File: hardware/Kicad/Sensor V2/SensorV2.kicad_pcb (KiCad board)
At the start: 2 copper layers, 82.4 x 64 mm, 20 parts, among them J1 Controller Connector, J2 Conn_01x08, J3 Conn_01x08, J4 Conn_01x06, J5 Conn_01x06, J6 Conn_01x04, U1 2821, U4 MicroSD_Breakout

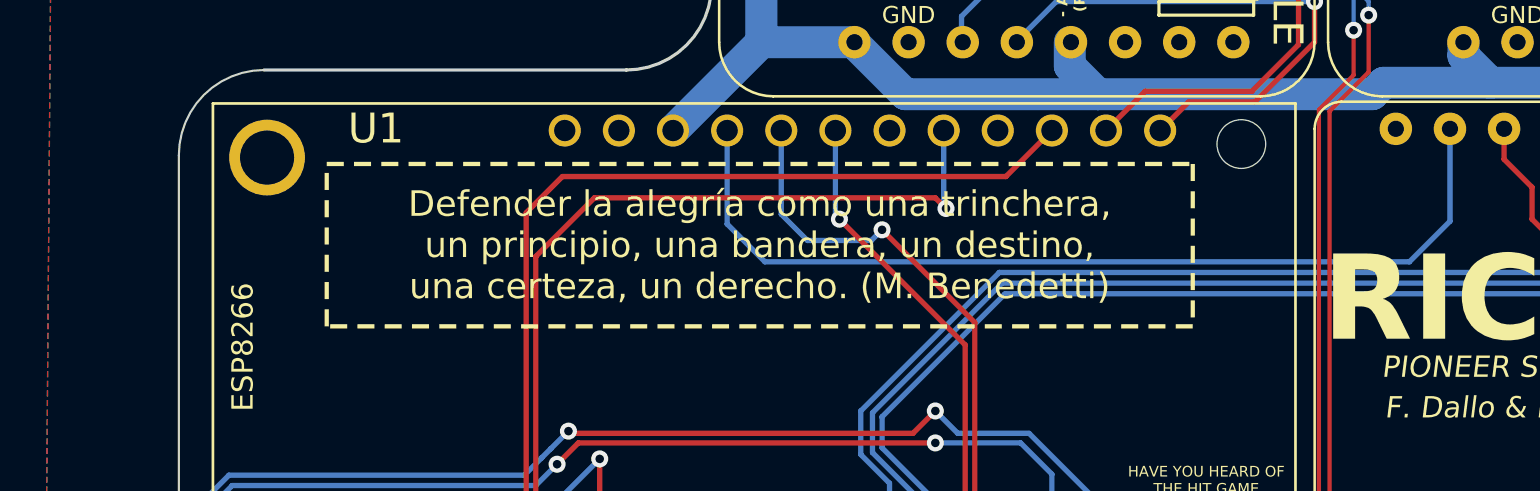
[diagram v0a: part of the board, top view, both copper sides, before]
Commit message: fixed CS to gpio16
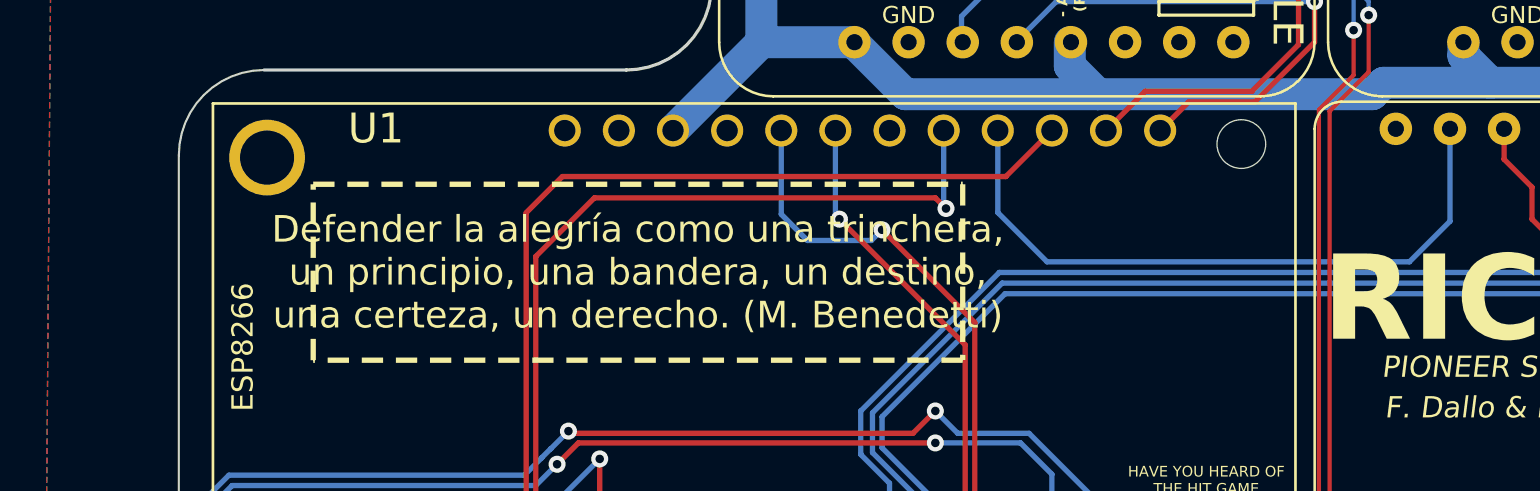
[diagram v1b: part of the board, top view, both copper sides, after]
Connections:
- U1 pad 20: /CS1 -> unconnected-(U1-GPIO14-Pad20)
- U1 pad 25: unconnected-(U1-GPIO16-Pad25) -> /CS1
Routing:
- net /CS1: track 44.2 -> 31.2 mm

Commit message: added some changes
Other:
- board text added: "ADC Addr: 0x49"
- board text removed: "ADC Addr: 0x40"
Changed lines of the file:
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@@
     (effects (font (size 0.8 0.8) (thickness 0.15)))
+  )
+  (gr_text "RX(Board)" (at 28.575 130.81) (layer "F.SilkS")
+    (effects (font (size 0.8 0.8) (thickness 0.15)))
+  )
+  (gr_text "F. Dallo & N. Zhao" (at 83.82 116.84) (layer "F.SilkS")
+    (effects (font (size 1 1) (thickness 0.15) italic))
+  )
+  (gr_text "RTC Only" (at 97.79 97.155) (layer "F.SilkS")
+    (effects (font (size 0.8 0.8) (thickness 0.15)))
+  )
+  (gr_text "- ADDR \n     (RTC NC)" (at 62.865 97.155 90) (layer "F.SilkS")
+    (effects (font (size 0.5 0.5) (thickness 0.1) bold))
+  )
+  (gr_text "ADC Addr: 0x48" (at 88.265 89.535) (layer "F.SilkS")
+    (effects (font (size 1.5 1.5) (thickness 0.25) bold))
+  )
+  (gr_text "TO MAIN" (at 21.59 131.445 270) (layer "F.SilkS")
+    (effects (font (size 1 1) (thickness 0.15)))
+  )
+  (gr_text "GND" (at 40.005 132.715) (layer "F.SilkS")
+    (effects (font (size 0.8 0.8) (thickness 0.15)))
+  )
+  (gr_text "GND" (at 83.82 98.425) (layer "F.SilkS")
+    (effects (font (size 0.8 0.8) (thickness 0.15)))
+  )
+  (gr_text "ADC MODULE" (at 73.025 93.345 270) (layer "F.SilkS")
+    (effects (font (size 1.4 1.4) (thickness 0.2)))
   )
   (gr_text "- ADDR \n     (RTC NC)" (at 91.44 97.155 90) (layer "F.SilkS")
     (effects (font (size 0.5 0.5) (thickness 0.1) bold))
-  )
-  (gr_text "RX(Board)" (at 28.575 130.81) (layer "F.SilkS")
-    (effects (font (size 0.8 0.8) (thickness 0.15)))
-  )
-  (gr_text "F. Dallo & N. Zhao" (at 83.82 116.84) (layer "F.SilkS")
-    (effects (font (size 1 1) (thickness 0.15) italic))
-  )
-  (gr_text "RTC Only" (at 97.79 97.155) (layer "F.SilkS")
-    (effects (font (size 0.8 0.8) (thickness 0.15)))
-  )
-  (gr_text "- ADDR \n     (RTC NC)" (at 62.865 97.155 90) (layer "F.SilkS")
-    (effects (font (size 0.5 0.5) (thickness 0.1) bold))
-  )
-  (gr_text "ADC Addr: 0x48" (at 88.265 89.535) (layer "F.SilkS")
-    (effects (font (size 1.5 1.5) (thickness 0.25) bold))
-  )
-  (gr_text "TO MAIN" (at 21.59 131.445 270) (layer "F.SilkS")
-    (effects (font (size 1 1) (thickness 0.15)))
-  )
-  (gr_text "GND" (at 40.005 132.715) (layer "F.SilkS")
-    (effects (font (size 0.8 0.8) (thickness 0.15)))
-  )
-  (gr_text "GND" (at 83.82 98.425) (layer "F.SilkS")
-    (effects (font (size 0.8 0.8) (thickness 0.15)))
-  )
-  (gr_text "ADC MODULE" (at 73.025 93.345 270) (layer "F.SilkS")
-    (effects (font (size 1.4 1.4) (thickness 0.2)))
   )
   (gr_text "GND" (at 70 76.5 180) (layer "F.SilkS")
@@
     (effects (font (size 1 1) (thickness 0.15) italic))
   )
-  (gr_text "ADC Addr: 0x40" (at 59.69 89.535) (layer "F.SilkS")
+  (gr_text "ADC Addr: 0x49" (at 59.69 89.535) (layer "F.SilkS")
     (effects (font (size 1.5 1.5) (thickness 0.25) bold))
   )

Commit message: more PCB updates
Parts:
- removed U2: ~, Adafruit_Sensors:ADCRTC_Dual
- added G***: LOGO, LOGO, F.Cu at (85.1, 124.5)
- added U5: 4Channel_ADC_Breakout, Adafruit_Sensors:4Channel ADC Breakout, F.Cu at (87.6, 84.5)
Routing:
- net /A3N: track 70.8 -> 69.5 mm
- net /A3P: track 73.5 -> 72.4 mm
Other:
- board text added: "ADC/RTC MODULE"
- board text added: "RICK"
- board text removed: "RICK .v2"

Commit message: feat: last kicad updates before sending order
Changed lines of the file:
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@@
     (fp_line (start 14.95 3.4) (end 14.95 -2.35)
       (stroke (width 0.1) (type solid)) (layer "F.Fab"))
-    (pad "1" thru_hole roundrect (at 0 0 180) (size 1.7 1.95) (drill 0.95) (layers "*.Cu" "*.Mask") (roundrect_rratio 0.147059)
+    (pad "1" thru_hole roundrect (at 0 0 180) (size 1.7 1.95) (drill 0.95) (layers "*.Cu" "*.Mask") (roundrect_rratio 0.1470588235)
       (net 2 "GND") (pinfunction "Pin_1") (pintype "passive"))
     (pad "2" thru_hole oval (at 2.5 0 180) (size 1.7 1.95) (drill 0.95) (layers "*.Cu" "*.Mask")
@@
     (fp_line (start 14.95 3.4) (end 14.95 -2.35)
       (stroke (width 0.1) (type solid)) (layer "F.Fab"))
-    (pad "1" thru_hole roundrect (at 0 0 180) (size 1.7 1.95) (drill 0.95) (layers "*.Cu" "*.Mask") (roundrect_rratio 0.147059)
+    (pad "1" thru_hole roundrect (at 0 0 180) (size 1.7 1.95) (drill 0.95) (layers "*.Cu" "*.Mask") (roundrect_rratio 0.1470588235)
       (net 2 "GND") (pinfunction "Pin_1") (pintype "passive"))
     (pad "2" thru_hole oval (at 2.5 0 180) (size 1.7 1.95) (drill 0.95) (layers "*.Cu" "*.Mask")
@@
       (stroke (width 0.1) (type solid)) (layer "F.Fab"))
     (pad "" np_thru_hole circle (at -1.6 2 180) (size 1.2 1.2) (drill 1.2) (layers "*.Cu" "*.Mask"))
-    (pad "1" thru_hole roundrect (at 0 0 180) (size 1.7 1.95) (drill 0.95) (layers "*.Cu" "*.Mask") (roundrect_rratio 0.147059)
+    (pad "1" thru_hole roundrect (at 0 0 180) (size 1.7 1.95) (drill 0.95) (layers "*.Cu" "*.Mask") (roundrect_rratio 0.1470588235)
       (net 22 "/A3P") (pinfunction "Pin_1") (pintype "passive"))
     (pad "2" thru_hole oval (at 2.5 0 180) (size 1.7 1.95) (drill 0.95) (layers "*.Cu" "*.Mask")
